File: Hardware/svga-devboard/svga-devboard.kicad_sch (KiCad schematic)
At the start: 4 parts

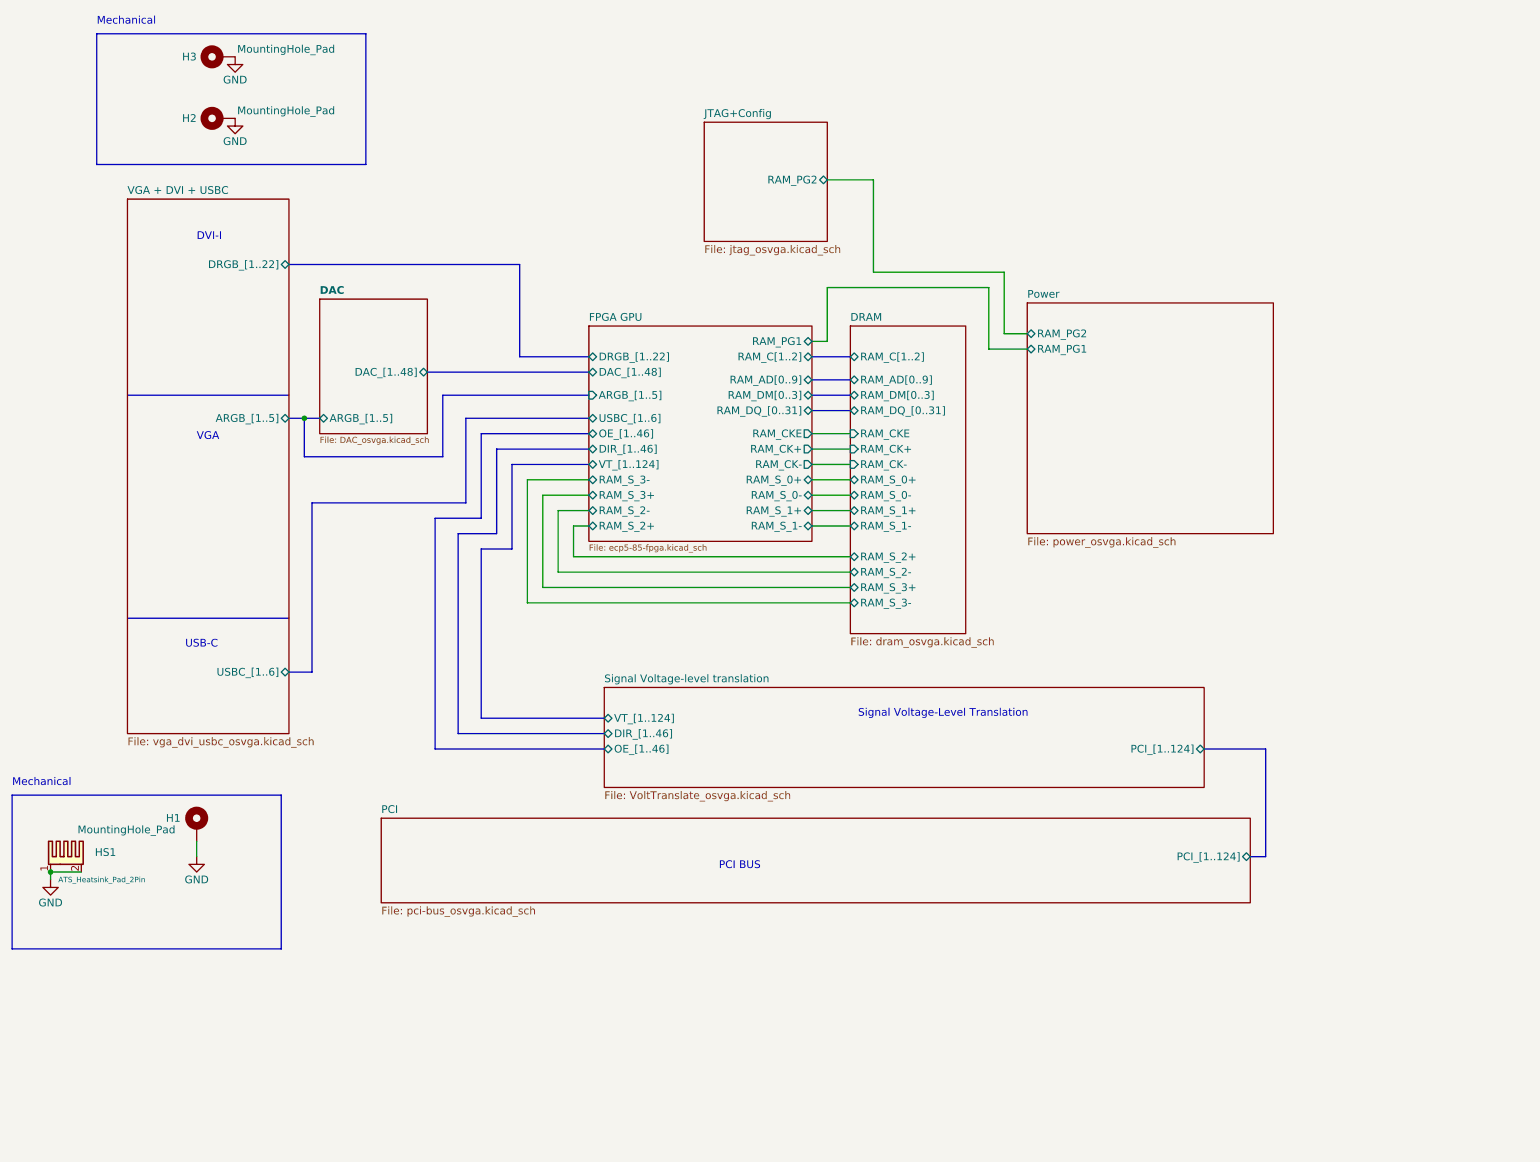
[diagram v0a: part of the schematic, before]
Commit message: Disconnected the DVI-connectors from each other, so that they do go over the intended flat-cable to the daughter-board instead.
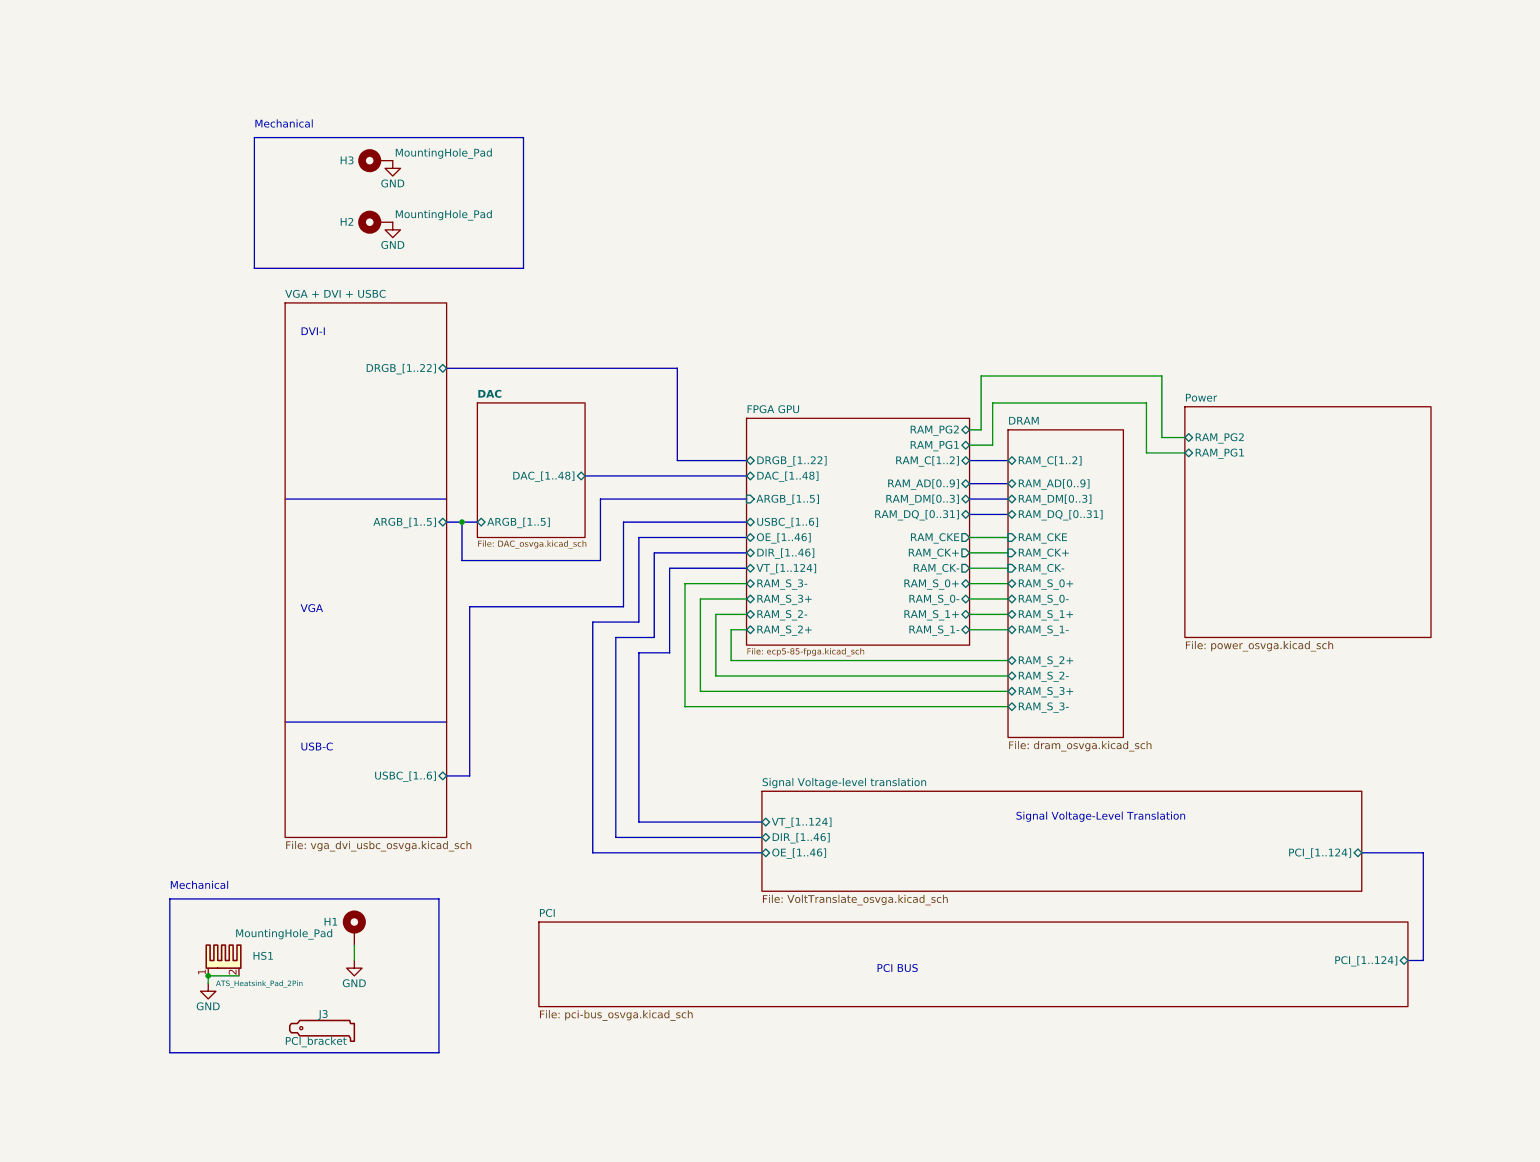
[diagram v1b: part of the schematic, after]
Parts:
- added J3: PCI_bracket, LRJ:PCI-card_bracket, symbol LRJ-parts:PCI-bracket
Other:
- removed sheet JTAG+Config
- sheet FPGA GPU ports: added RAM_PG2; removed none
- moved on the sheet: H1, H2, H3, HS1
